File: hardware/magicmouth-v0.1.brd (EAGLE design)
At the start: 100 x 80 mm, 36 parts, among them IC1 LM386N, IC2 ATMEGA328P_PDIP, J2 AUDIO-JACK2PTH, Q1 16Mhz, U1 ARDUINOR3-NOIOREF-NOTEXT

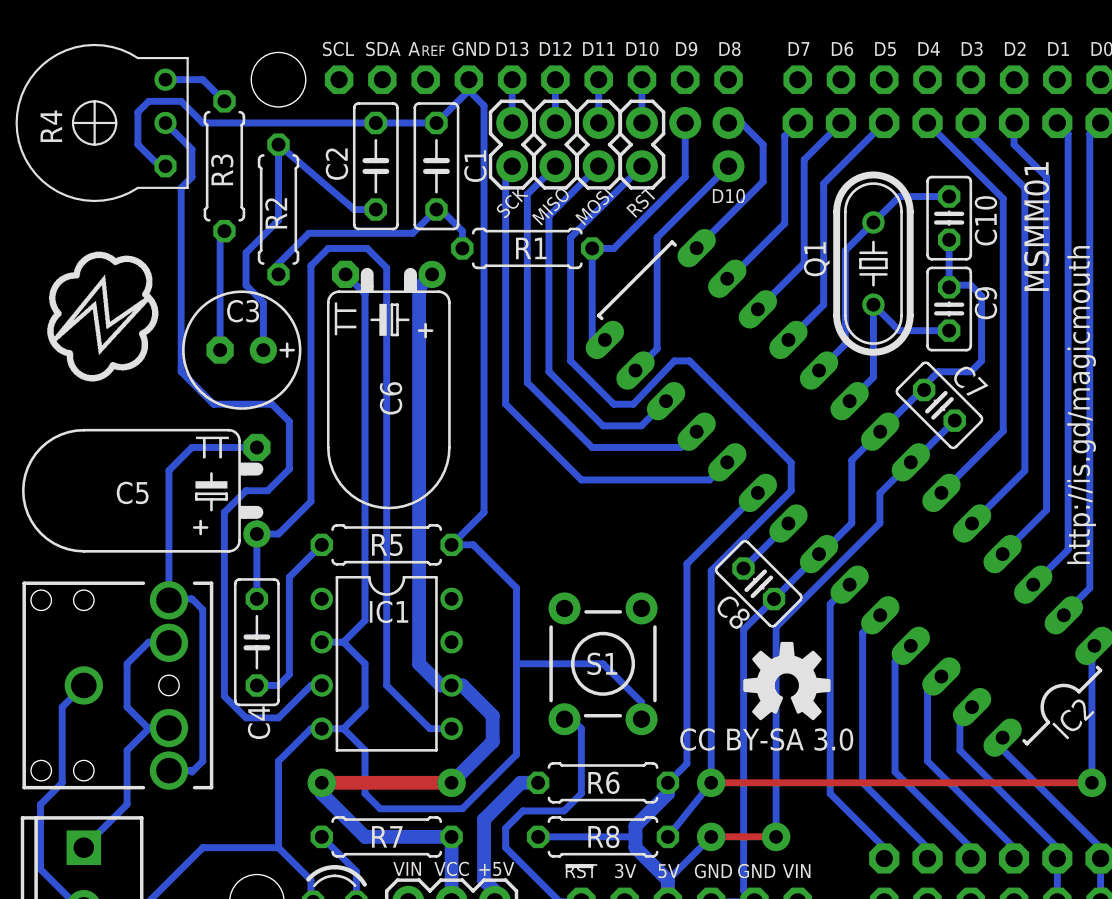
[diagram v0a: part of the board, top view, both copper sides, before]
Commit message: 10uf bypass cap for LM386
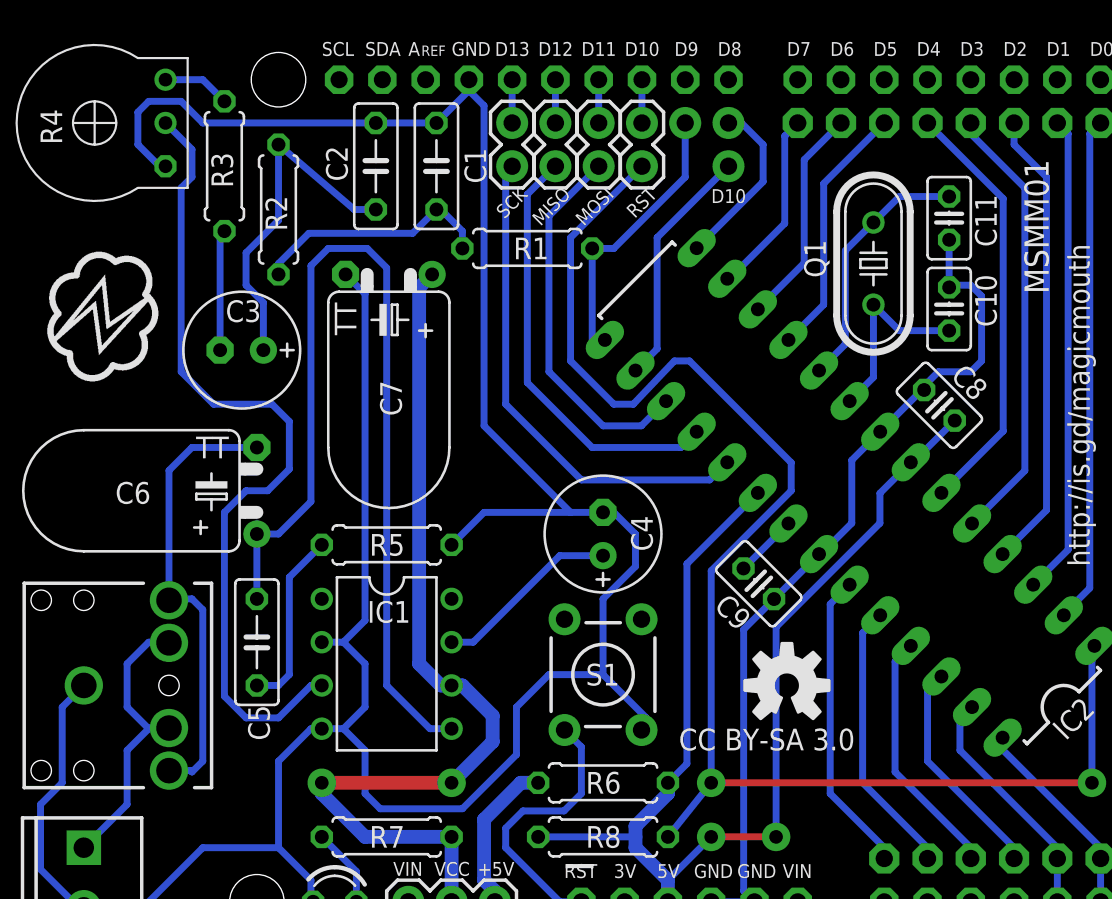
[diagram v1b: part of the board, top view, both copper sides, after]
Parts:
- added C11: 22pF, rcl:C025-025X050
- C4: value 47nF -> 10uF; device resistor:C050-025X075 -> rcl:E2,5-7
- C5: value 220uF -> 47nF; device rcl:TT5D7L -> resistor:C050-025X075
- C7: value 100nF -> 220uF; device rcl:C025-025X050 -> rcl:TT5D7L
- C9: value 22pF -> 100nF
- moved C7 33.2 mm to (31.9, 49.5), turned to 180 degrees
- moved C4 21.3 mm to (44.5, 34.3), turned to 90 degrees
- moved C9 19.6 mm to (53.6, 31.4), turned to 315 degrees
- moved C8 14.9 mm to (64.2, 41.8), turned to 135 degrees
- moved C6 14.9 mm to (24.1, 36.8), turned to 90 degrees
- moved C5 8.89 mm to (24.1, 27.9), turned to 270 degrees
- moved C10 5.33 mm to (64.8, 47.5)
- moved S1 0.64 mm to (44.5, 26.0)
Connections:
- new net N$33: C4.+, IC1.7
- net +5V: now also C8.1; no longer C7.1
- net GND: now also C4.-, C7.-; no longer C6.-
- net GND1: now also C10.1, C11.2, C9.2; no longer C10.2, C7.2, C9.1
- net N$1: now also C5.1, C6.+; no longer C4.1, C5.+
- net N$11: now also C11.1; no longer C10.1
- net N$34: now also C9.1; no longer C8.1
- net N$4: now also C5.2; no longer C4.2
- net N$6: now also C10.2; no longer C9.2
- net N$8: now also C6.-; no longer C5.-
- net VCC: now also C7.+; no longer C6.+
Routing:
- net N$33: track 0.00 -> 11.0 mm
- net GND: track 164.5 -> 174.3 mm
- net N$35: track 17.2 -> 16.3 mm
